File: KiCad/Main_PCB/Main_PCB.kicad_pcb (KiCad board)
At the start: 2 copper layers, 75 x 15 mm, 50 parts, among them IC1 AP3602, J1 USB_C_Receptacle_USB2.0_14P, J3 Video Out, Q1 S8050, Q2 S8050, SW3 Main Power, U1 CP2102N-Axx-xQFN28, U2 ESP32-PICO-D4, U3 MCP73831-2-OT, U4 AMS1117

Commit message: Changed Footprints
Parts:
- J1: footprint Connector_USB:USB_C_Receptacle_Amphenol_12401548E4-2A -> Connector_USB:USB_C_Receptacle_GCT_USB4085
- Q1, Q2: footprint Package_TO_SOT_THT:TO-92_Inline -> Package_TO_SOT_SMD:SOT-23
- SW3: footprint Button_Switch_SMD:SW_DIP_SPSTx01_Slide_6.7x4.1mm_W6.73mm_P2.54mm_LowProfile_JPin -> Button_Switch_SMD:SW_DIP_SPSTx01_Slide_Copal_CHS-01B_W7.62mm_P1.27mm
- moved BT1 23.6 mm to (145.6, 64.5), turned to 90 degrees
- moved Q1 23.2 mm to (163.6, 81.0)
- moved Q2 23.2 mm to (156.6, 81.0)
- moved D1 20.3 mm to (173.7, 85.5)
- moved D3 20.3 mm to (169.1, 85.0)
- moved D2 19.1 mm to (173.7, 88.5)
- moved D4 18.5 mm to (169.6, 88.5)
- moved IC1 11.1 mm to (139.4, 71.0)
- moved SW2 10.2 mm to (155.5, 71.0)
- moved SW3 9.29 mm to (158.4, 89.5)
- moved SW1 8.46 mm to (148.5, 71.0)
- moved U1 4.86 mm to (153.0, 62.5)
- moved J1 3.10 mm to (163.6, 67.0)
- moved U4 0.50 mm to (133.5, 63.0)

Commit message: PCB update
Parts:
- removed C13, C14, C15: 10uF, Capacitor_SMD:C_0402_1005Metric
- removed IC1: AP3602, Package_TO_SOT_SMD:SOT-23-6
- removed J3: Video Out, Connector_Wire:SolderWire-0.1sqmm_1x01_D0.4mm_OD1mm
- removed R14: 2K, Resistor_SMD:R_0402_1005Metric
- added J2: Display, Connector_Wire:SolderWire-0.1sqmm_1x04_P3.6mm_D0.4mm_OD1mm, F.Cu at (158.9, 42.4)
- C10: value 1uf -> 10uF
- C12: value 10uf -> 0.1uF
- C4: value 4.7pF -> 0.1uF
- C5: value 0.1uF -> 4.7pF
- C8: value 0.1uF -> 10uF
- C9: value 10uF -> 10uf
- L1: footprint Inductor_SMD:L_1206_3216Metric -> Inductor_SMD:L_0603_1608Metric
- R12: value 100K -> 10K; footprint Resistor_SMD:R_0603_1608Metric -> Resistor_SMD:R_0402_1005Metric
- R13, R3: value 10K -> 2K
- R4: value 2K -> 10K
- moved C5 90.0 mm to (172.2, 42.3), turned to -90 degrees
- moved E1 82.8 mm to (179.4, 48.3)
- moved C3 72.3 mm to (162.6, 54.4), turned to -90 degrees
- moved L1 70.7 mm to (175.1, 42.7), turned to -90 degrees
- moved C1 69.8 mm to (160.8, 49.9), turned to 180 degrees
- moved C4 68.4 mm to (149.2, 44.2)
- moved C6 67.1 mm to (160.8, 45.3), turned to 180 degrees
- moved D2 64.8 mm to (123.4, 47.7), turned to -90 degrees
- moved C2 63.0 mm to (149.2, 46.4), turned to 180 degrees
- moved C7 62.9 mm to (154.2, 46.0), turned to 180 degrees
- moved R4 61.5 mm to (160.8, 48.7)
- moved R10 61.4 mm to (160.8, 46.4)
- moved R5 61.1 mm to (149.2, 42.0)
- moved D1 60.3 mm to (126.7, 47.7), turned to -90 degrees
- moved C10 58.9 mm to (134.8, 42.8), turned to 180 degrees
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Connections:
- C10 pad 1: Net-(IC1-C+) -> Net-(BT1-+)
- C10 pad 2: Net-(IC1-C-) -> GND
- C11 pad 1: +3.7V Bat -> +3.3V
- C12 pad 1: GND -> /EN
- C12 pad 2: +5V USB -> GND
- C4 pad 1: Net-(U2-LNA_IN) -> +3.3V
- C4 pad 2: Net-(C3-Pad1) -> GND
- C5 pad 1: +3.3V -> Net-(U2-LNA_IN)
- C5 pad 2: GND -> Net-(C3-Pad1)
- C8 pad 1: /EN -> +3.7V Bat
- C9 pad 1: +3.3V -> GND
- C9 pad 2: GND -> +5V USB
- D3 pad 1: Net-(D3-K) -> +5V USB
- R12 pad 1: /~{SHDN} -> Net-(U3-STAT)
- R12 pad 2: +3.3V -> Net-(GREEN1-A)
- R13 pad 2: Net-(GREEN1-A) -> Net-(RED1-K)
- R3 pad 2: Net-(U2-EN) -> Net-(U1-~{RST})
- R4 pad 2: Net-(U1-~{RST}) -> Net-(U2-EN)
- SW3 pad 2: Net-(SW3-B) -> +3.7V Bat
- U2 pad 14: Net-(J3-Pin_1) -> unconnected-(U2-IO25-Pad14)
- U2 pad 39: unconnected-(U2-IO22-Pad39) -> /SCL
- U2 pad 42: unconnected-(U2-IO21-Pad42) -> /SDA
- U4 pad 2: Net-(U4-VO) -> +3.3V
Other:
- board size 75 x 15 mm -> 60 x 15 mm
- copper layers 2 -> 4

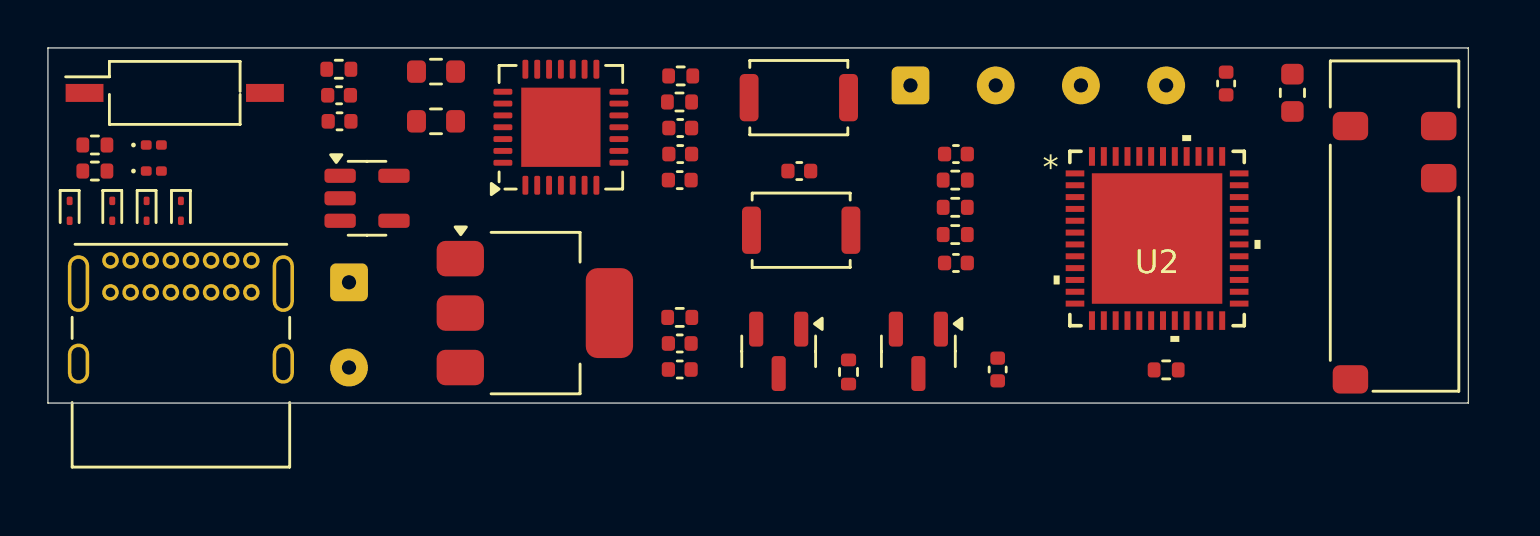
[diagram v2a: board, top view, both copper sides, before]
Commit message: Most traces done
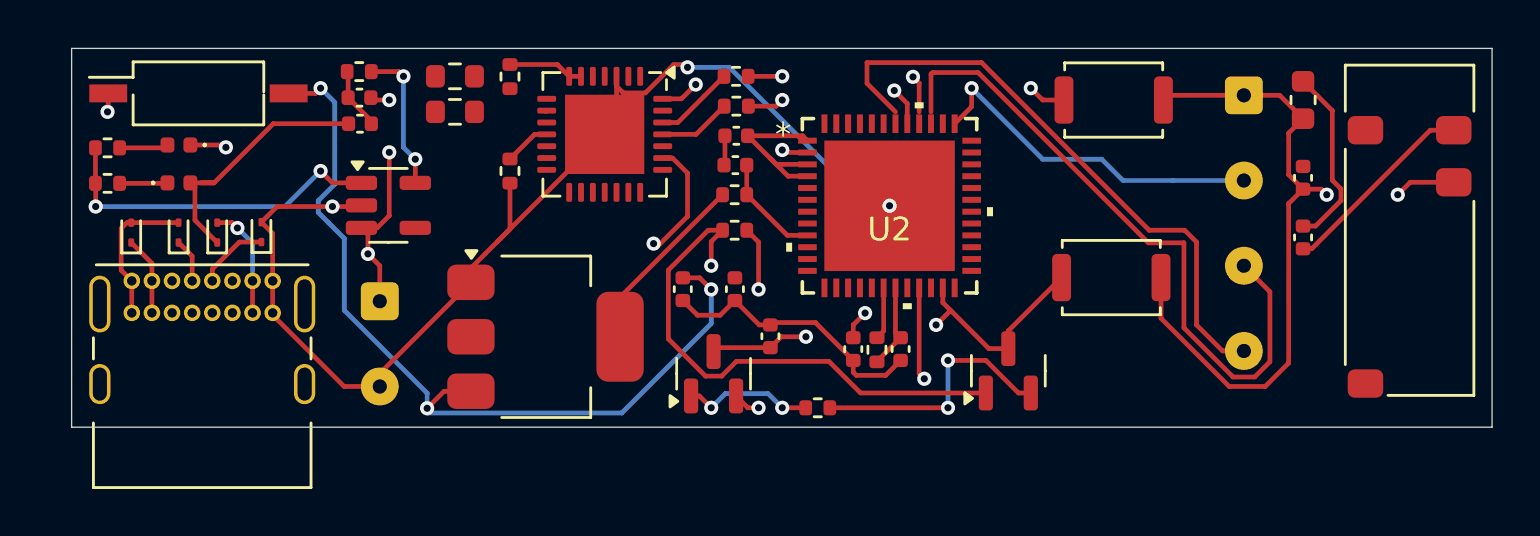
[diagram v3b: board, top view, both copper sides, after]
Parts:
- removed C6: 0.1uF, Capacitor_SMD:C_0402_1005Metric
- GREEN1, RED1: footprint LED_SMD:LED_0201_0603Metric -> LED_SMD:LED_0402_1005Metric
- moved C3 15.2 mm to (175.5, 46.3)
- moved J2 14.1 mm to (173.0, 42.8), turned to -90 degrees
- moved SW2 13.3 mm to (167.5, 43.0), turned to 180 degrees
- moved SW1 13.3 mm to (167.4, 50.5), turned to 180 degrees
- moved C4 13.2 mm to (158.5, 53.5), turned to -90 degrees
- moved R6 12.2 mm to (157.5, 53.5), turned to 90 degrees
- moved U2 11.4 mm to (158.0, 47.5)
- moved R10 10.2 mm to (151.6, 42.0)
- moved C1 10.2 mm to (151.5, 45.8)
- moved R9 10.2 mm to (151.6, 43.3)
- moved R4 9.47 mm to (151.5, 47.0)
- moved C12 8.59 mm to (153.0, 53.0), turned to 90 degrees
- moved R5 8.25 mm to (142.0, 46.0), turned to -90 degrees
- moved D2 8.15 mm to (131.5, 48.6), turned to 90 degrees
- moved C7 7.86 mm to (156.5, 53.5), turned to -90 degrees
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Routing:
- net GND: track 0.00 -> 113.6 mm, vias 0 -> 6
- net +3.3V: track 0.00 -> 37.0 mm, vias 0 -> 1
- net +3.7V Bat: track 0.00 -> 36.2 mm, vias 0 -> 3
- net Net-(U2-LNA_IN): track 0.00 -> 32.8 mm, vias 0 -> 1
- net /DTR: track 0.00 -> 32.0 mm, vias 0 -> 2
- net /SCL: track 0.00 -> 28.1 mm
- net /SDA: track 0.00 -> 25.6 mm
- net Net-(BT1-+): track 0.00 -> 24.9 mm, vias 0 -> 4
- net /CTS: track 0.00 -> 24.1 mm, vias 0 -> 2
- net /EN: track 0.00 -> 20.2 mm, vias 0 -> 2
- net Net-(U3-STAT): track 0.00 -> 14.5 mm, vias 0 -> 2
- net /IO0: track 0.00 -> 13.4 mm, vias 0 -> 2
- net +5V USB: track 0.00 -> 11.3 mm
- net Net-(Q2-B): track 0.00 -> 11.1 mm, vias 0 -> 2
- net Net-(Q1-B): track 0.00 -> 8.86 mm, vias 0 -> 2
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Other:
- board size 60 x 15 mm -> 60 x 16 mm
- board text added: "Boot"
- board text added: "Reset"

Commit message: Update
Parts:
- moved U1 0.60 mm to (146.0, 45.0)
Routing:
- net GND: track 113.6 -> 147.2 mm, vias 6 -> 11
- net /USB_DN: track 3.04 -> 22.6 mm, vias 0 -> 2
- net /RTS: track 5.54 -> 19.7 mm, vias 2 -> 4
- net +5V USB: track 11.3 -> 20.7 mm
- net Net-(U1-VBUS): track 0.00 -> 4.94 mm
- net Net-(U1-~{RST}): track 0.09 -> 4.60 mm, vias 0 -> 2
- net /USB_DP: track 1.86 -> 2.87 mm, vias 0 -> 1
- net /TXD: track 3.40 -> 4.19 mm
- net /DTR: track 32.0 -> 31.3 mm
- net +3.3V: track 37.0 -> 37.8 mm
- net /CTS: track 24.1 -> 23.5 mm

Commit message: Different layout attempt
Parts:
- moved RED1 86.5 mm to (196.0, 100.0)
- moved GREEN1 86.3 mm to (196.0, 98.0), turned to 0 degrees
- moved R13 85.7 mm to (192.0, 100.0)
- moved R12 85.1 mm to (192.0, 97.5)
- moved C10 67.4 mm to (173.0, 99.0), turned to 0 degrees
- moved C9 65.6 mm to (175.0, 96.5), turned to 0 degrees
- moved R11 65.1 mm to (171.0, 96.5), turned to 0 degrees
- moved C1 64.1 mm to (138.5, 108.5), turned to 0 degrees
- moved R4 63.5 mm to (135.5, 108.5)
- moved R3 63.3 mm to (135.5, 105.0), turned to 0 degrees
- moved R6 62.0 mm to (135.5, 111.5), turned to 0 degrees
- moved C2 61.7 mm to (139.5, 105.0), turned to 0 degrees
- moved R5 52.2 mm to (146.5, 98.0), turned to 0 degrees
- moved SW2 50.6 mm to (153.0, 91.5)
- moved C4 49.0 mm to (146.5, 101.0), turned to 0 degrees
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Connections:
- C1 pad 1: Net-(U2-EN) -> /EN
- R4 pad 2: Net-(U2-EN) -> /EN
- U2 pad 9: Net-(U2-EN) -> /EN
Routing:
- net GND: track 147.2 -> 91.8 mm, vias 11 -> 3
- net Net-(U2-LNA_IN): track 32.8 -> 0.00 mm, vias 1 -> 0
- net +3.7V Bat: track 36.2 -> 6.85 mm, vias 3 -> 0
- net /DTR: track 31.3 -> 11.3 mm
- net +5V USB: track 20.7 -> 1.70 mm
- net /IO0: track 13.4 -> 29.8 mm
- net /CTS: track 23.5 -> 7.31 mm, vias 2 -> 0
- net /USB_DP: track 2.87 -> 18.8 mm, vias 1 -> 2
- net Net-(U3-STAT): track 14.5 -> 0.00 mm, vias 2 -> 0
- net /SCL: track 28.1 -> 15.9 mm, vias 0 -> 1
- net Net-(Q2-B): track 11.1 -> 0.00 mm, vias 2 -> 0
- net Net-(Q1-B): track 8.86 -> 0.00 mm, vias 2 -> 0
- net Net-(C3-Pad1): track 8.44 -> 0.00 mm
- net /RXD0: track 8.56 -> 16.9 mm
- net /SDA: track 25.6 -> 17.7 mm, vias 0 -> 1
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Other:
- board size 60 x 16 mm -> 60 x 18 mm
- board text removed: "Boot"
- board text removed: "Reset"

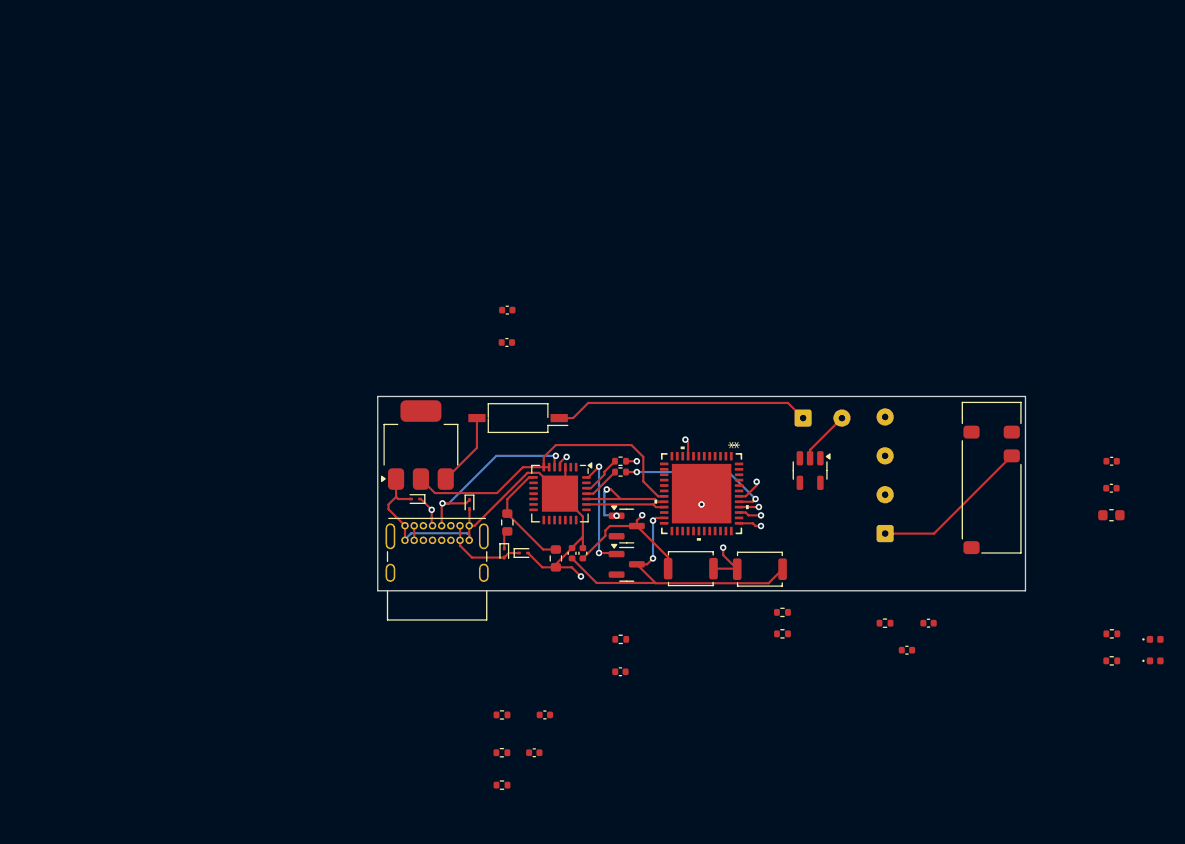
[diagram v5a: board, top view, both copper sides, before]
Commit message: Added Ground plane and Migrated Libraries
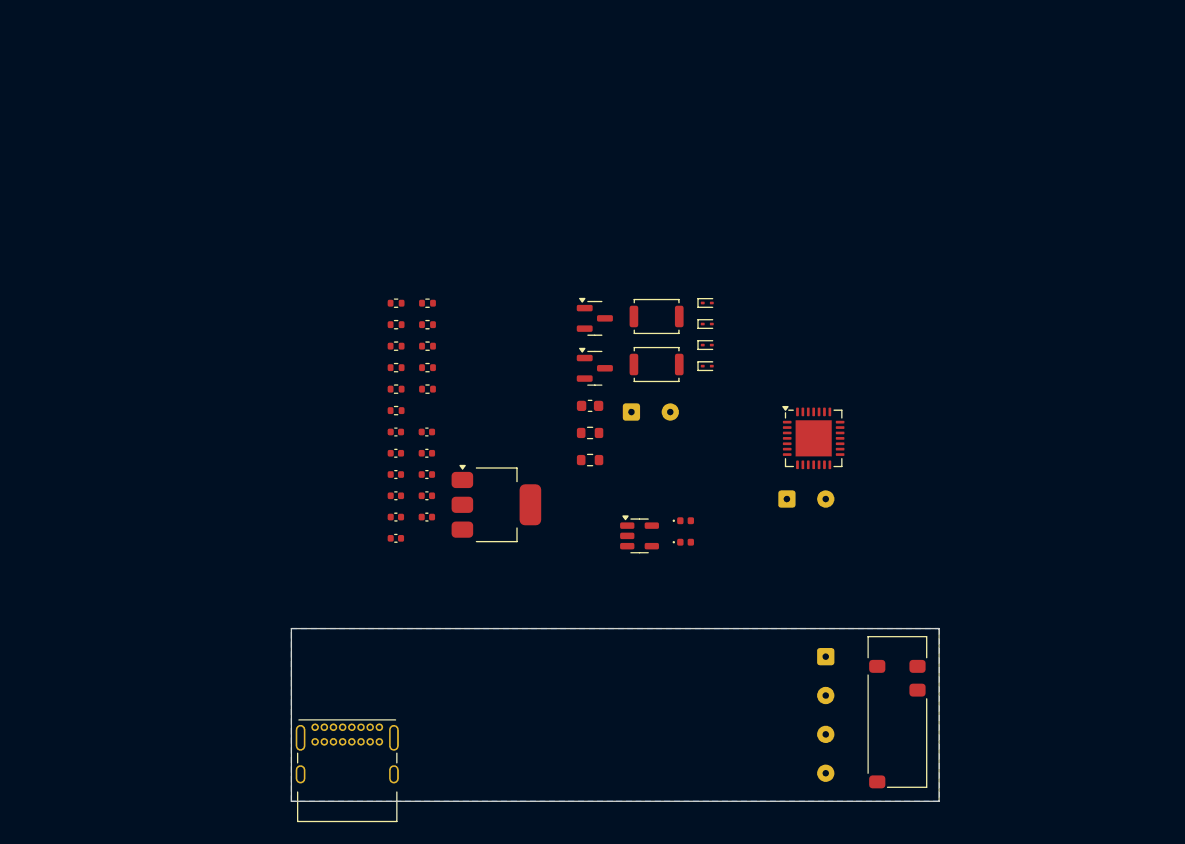
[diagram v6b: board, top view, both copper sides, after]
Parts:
- removed U2: ESP32-PICO-D4, ESP32 PICO D4:ESP32-PICO-D4_EXP
- SW3: footprint Button_Switch_SMD:SW_DIP_SPSTx01_Slide_Copal_CHS-01B_W7.62mm_P1.27mm -> Connector_Wire:SolderWire-0.1sqmm_1x02_P3.6mm_D0.4mm_OD1mm
- moved R13 68.2 mm to (128.6, 74.8)
- moved R12 68.0 mm to (128.6, 72.8)
- moved C5 66.5 mm to (125.7, 86.7)
- moved C3 66.3 mm to (125.7, 82.7)
- moved R11 49.5 mm to (128.6, 70.8)
- moved L1 49.3 mm to (143.7, 76.4)
- moved C9 49.1 mm to (128.6, 80.8)
- moved C10 47.4 mm to (128.6, 82.7)
- moved GREEN1 44.9 mm to (152.5, 87.0)
- moved RED1 44.9 mm to (152.5, 89.0)
- moved R7 41.3 mm to (125.7, 74.8)
- moved R8 41.3 mm to (125.7, 76.8)
- moved R4 40.8 mm to (125.7, 68.8)
- moved R6 39.9 mm to (125.7, 72.8)
- moved R3 39.4 mm to (125.7, 66.9)
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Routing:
- net GND: track 91.8 -> 0.00 mm, vias 3 -> 0
- net +3.3V: track 44.1 -> 0.00 mm, vias 1 -> 0
- net /IO0: track 29.8 -> 0.00 mm, vias 2 -> 0
- net /EN: track 26.1 -> 0.00 mm, vias 2 -> 0
- net Net-(BT1-+): track 23.7 -> 0.00 mm
- net /USB_DP: track 18.8 -> 0.00 mm, vias 2 -> 0
- net /USB_DN: track 18.2 -> 0.00 mm, vias 2 -> 0
- net /SDA: track 17.7 -> 0.00 mm, vias 1 -> 0
- net /RXD0: track 16.9 -> 0.00 mm, vias 2 -> 0
- net /SCL: track 15.9 -> 0.00 mm, vias 1 -> 0
- net /TXD0: track 14.7 -> 0.00 mm, vias 2 -> 0
- net /RTS: track 12.6 -> 0.00 mm, vias 2 -> 0
- net /DTR: track 11.3 -> 0.00 mm, vias 2 -> 0
- net Net-(U1-VBUS): track 10.5 -> 0.00 mm
- net Net-(D1-A1): track 9.36 -> 0.00 mm
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- added copper zone on B.Cu, net GND
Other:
- board size 60 x 18 mm -> 60 x 16 mm

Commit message: Ground plane
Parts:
- added U2: ESP32-PICO-D4, ESP32 PICO D4:ESP32-PICO-D4_EXP, F.Cu at (155.0, 105.0)
- SW3: value Main Power -> M-Switch
- moved R8 63.2 mm to (188.5, 84.4)
- moved R7 63.2 mm to (188.5, 82.1)
- moved C10 50.2 mm to (177.2, 70.6)
- moved R12 49.3 mm to (177.9, 73.9)
- moved R13 49.2 mm to (177.8, 75.8)
- moved SW3 46.5 mm to (117.3, 98.3)
- moved R11 44.6 mm to (173.2, 70.4)
- moved C7 43.9 mm to (169.2, 82.9)
- moved Q1 42.7 mm to (184.2, 82.9)
- moved Q2 42.7 mm to (184.2, 87.5)
- moved C12 40.6 mm to (169.1, 87.5)
- moved R9 40.1 mm to (144.7, 103.6)
- moved U1 39.1 mm to (137.2, 107.5)
- moved SW1 38.4 mm to (144.6, 106.1)
- moved SW2 37.7 mm to (144.5, 109.9)
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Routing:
- net GND: track 0.00 -> 1.90 mm, vias 0 -> 1

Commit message: Pre JLC Check
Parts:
- removed C12: 0.1uF, Capacitor_SMD:C_0402_1005Metric
- removed the C4 at (147.3, 88.2)
- removed the C8 at (133.1, 97.7)
- removed the C9 at (129.2, 80.6)
- added C10: 0.1uF, Capacitor_SMD:C_0402_1005Metric, F.Cu at (155.4, 110.7)
- added C4: 10uF, Capacitor_SMD:C_0402_1005Metric, F.Cu at (156.2, 99.2)
- added C4: 0.1uF, Capacitor_SMD:C_0402_1005Metric, F.Cu at (158.9, 99.2)
- added C6: 10uF, Capacitor_SMD:C_0402_1005Metric, F.Cu at (134.2, 101.8)
- C2: value 10uF -> 2.7pF
- C3: value 2.7pF -> 4.7pF
- C5: value 4.7pF -> 0.1uF
- C7: value 0.1uF -> 10uf
- L1: footprint Inductor_SMD:L_0603_1608Metric -> Inductor_SMD:L_0402_1005Metric
- SW3: value M-Switch -> Main Power
- moved C8 62.2 mm to (121.9, 98.9), turned to -90 degrees
- moved R12 61.7 mm to (123.6, 103.4)
- moved R11 60.6 mm to (121.7, 102.4), turned to -90 degrees
- moved R13 58.2 mm to (125.9, 102.2), turned to 180 degrees
- moved U3 57.1 mm to (118.7, 101.4), turned to -90 degrees
- moved RED1 56.6 mm to (123.6, 102.2), turned to 180 degrees
- moved GREEN1 56.3 mm to (125.8, 103.4)
- moved D1 51.9 mm to (119.2, 104.8), turned to 90 degrees
- moved R6 51.7 mm to (161.3, 110.8), turned to 90 degrees
- moved R7 50.4 mm to (146.3, 109.7), turned to 90 degrees
- moved D3 50.4 mm to (117.5, 104.9), turned to -90 degrees
- moved R8 48.3 mm to (147.4, 109.7), turned to -90 degrees
- moved D2 48.2 mm to (122.4, 104.8), turned to 90 degrees
- moved C7 47.0 mm to (125.2, 99.5)
- moved D4 46.5 mm to (120.8, 104.8), turned to 90 degrees
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- renumbered C10 to C8, C11 to C9
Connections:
- C2 pad 1: +3.3V -> Net-(C2-Pad1)
- C3 pad 1: Net-(C3-Pad1) -> Net-(U2-LNA_IN)
- C3 pad 2: GND -> Net-(C2-Pad1)
- C5 pad 1: Net-(U2-LNA_IN) -> /IO0
- C5 pad 2: Net-(C3-Pad1) -> GND
- C7 pad 1: /IO0 -> GND
- C7 pad 2: GND -> +5V USB
- E1 pad 2: Net-(C3-Pad1) -> Net-(C2-Pad1)
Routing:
- net +3.3V: track 0.00 -> 113.2 mm, vias 0 -> 5
- net GND: track 1.90 -> 98.5 mm, vias 1 -> 5
- net /IO0: track 0.00 -> 32.5 mm, vias 0 -> 2
- net /RTS: track 0.00 -> 31.9 mm, vias 0 -> 2
- net +5V USB: track 0.00 -> 28.3 mm, vias 0 -> 2
- net /CTS: track 0.00 -> 26.4 mm, vias 0 -> 2
- net /EN: track 0.00 -> 25.1 mm
- net /RXD0: track 0.00 -> 24.3 mm, vias 0 -> 2
- net /USB_DP: track 0.00 -> 23.6 mm, vias 0 -> 1
- net Net-(BT1-+): track 0.00 -> 21.6 mm
- net /TXD0: track 0.00 -> 21.4 mm, vias 0 -> 2
- net /USB_DN: track 0.00 -> 20.7 mm, vias 0 -> 2
- net Net-(U3-STAT): track 0.00 -> 15.4 mm
- net /SDA: track 0.00 -> 14.5 mm, vias 0 -> 1
- net Net-(C2-Pad1): track 0.00 -> 13.8 mm, vias 0 -> 2
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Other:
- board text added: "B+"
- board text added: "B-"
- board text added: "Reset"
